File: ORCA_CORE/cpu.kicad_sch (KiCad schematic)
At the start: 0 parts

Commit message: made all sketch for test (cpu board is only for test
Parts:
- added C40, C46, C47: 4.7u, symbol Device:C
- added C44, C48: 1u, symbol Device:C
- added C45: 0.1u, symbol Device:C
- added C49: 1u/50V, symbol Device:C
- added C50: 0.1u25V, symbol Device:C
- added D19: LED_cpu, symbol Device:LED_Filled
- added D20: LED_motor, symbol Device:LED_Filled
- added D22, D25: CUHS20560, symbol Device:D_Schottky
- added D23: LED_usb, symbol Device:D_Filled
- added D24: WS2812B, LED_SMD:LED_WS2812B_PLCC4_5.0x5.0mm_P3.2mm, symbol LED:WS2812B
- added J10: Raspberry_Pi_2_3, Connector_PinSocket_2.54mm:PinSocket_2x20_P2.54mm_Horizontal, symbol Connector:Raspberry_Pi_2_3
- added J11, J12: I2C, symbol Connector_Generic:Conn_01x03
- added J13: 6Vout, symbol Connector_Generic:Conn_01x02
- added J14, J20: 5Vout, symbol Connector_Generic:Conn_01x02
- added J15, J16: Conn_01x05_Pin, symbol Connector:Conn_01x05_Pin
- added P1: USB_C_Plug_USB2.0, symbol Connector:USB_C_Plug_USB2.0
- added Q6, Q7: BSS138, Package_TO_SOT_SMD:SOT-23, symbol Transistor_FET:BSS138
- added R34: 0, symbol Device:R
- added R35, R36, R40: 1k, symbol Device:R
- added R37, R38, R41, R42, R43, R44, R45, R46: 2.2k, symbol Device:R
- added R39: 5.1k, symbol Device:R
- added U13: FT230XS, Package_SO:SSOP-16_3.9x4.9mm_P0.635mm, symbol Interface_USB:FT230XS
- added U14: BNO055, symbol mylib:BNO055
- added U15: NJM78055DL1, symbol mylib:NJM7805SDL1
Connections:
- new net: D22.2 (A), P1.A4 (VBUS), P1.A9 (VBUS), P1.B4 (VBUS), P1.B9 (VBUS), R40.1
- new net: D23.2 (A), R40.2
- new net: P1.A5 (CC), R39.2
- new net: P1.A6 (D+), U13.8 (USBDP)
- new net: P1.A7 (D-), U13.9 (USBDM)
- new net: D20.2 (A), R36.2
- new net: D19.2 (A), R35.2
- new net +3V3_cpu: J10.1 (3V3), J10.17 (3V3), J11.1 (Pin_1), J12.1 (Pin_1), Q6.1 (G), Q7.1 (G), R37.1, R38.1, R41.1, R42.1, R43.1, R44.1, U14.1 (VDD), U14.2 (VDDIO)
- new net +5V_cpu: C40.1, C44.1, C45.1, D22.1 (K), D24.1 (VDD), J10.2 (5V), J10.4 (5V), J14.2 (Pin_2), R35.1, R45.1, R46.1, U13.12 (VCC), U13.3 (VCCIO)
- new net +5V_cpu2servo: C50.1, D25.2 (A), J20.2 (Pin_2), U15.2 (Vout)
- new net +6V_cpu: C46.1, C47.1, C48.1, C49.1, D25.1 (K), J13.2 (Pin_2), R36.1, U15.3 (Vin)
- new net GND: C40.2, C44.2, C45.2, C46.2, C47.2, C48.2, C49.2, C50.2, D19.1 (K), D20.1 (K), D23.1 (K), D24.3 (VSS), J10.14 (GND), J10.20 (GND), J10.25 (GND), J10.30 (GND), J10.34 (GND), J10.39 (GND), J10.6 (GND), J10.9 (GND), J13.1 (Pin_1), J14.1 (Pin_1), J20.1 (Pin_1), P1.A1 (GND), P1.A12 (GND), P1.B1 (GND), P1.B12 (GND), P1.S1 (SHIELD), R34.1, R34.2, R39.1, U13.13 (GND), U13.5 (GND), U14.10 (GND), U14.5 (ADOR), U14.8 (PS0), U14.9 (PS1), U15.1 (GND)
- new net GPIO12: J10.32 (PWM0/GPIO12), J15.1 (Pin_1)
- new net GPIO13: J10.33 (PWM1/GPIO13), J15.2 (Pin_2)
- new net GPIO16: J10.36 (GPIO16), J15.3 (Pin_3)
- new net GPIO17: J10.11 (GPIO17), J15.4 (Pin_4)
- new net GPIO18: J10.12 (GPIO18/PWM0), J15.5 (Pin_5)
- new net GPIO19: J10.35 (GPIO19/MISO1), J16.1 (Pin_1)
- new net GPIO20: J10.38 (GPIO20/MOSI1), J16.2 (Pin_2)
- new net GPIO21: J10.40 (GPIO21/SCLK1), J16.3 (Pin_3)
- new net GPIO26: J10.37 (GPIO26), J16.4 (Pin_4)
- new net GPIO27: J10.13 (GPIO27), J16.5 (Pin_5)
- new net RXD_3V3: J10.10 (GPIO15/RXD), Q7.2 (S), R44.2
- new net RXD_5V: Q7.3 (D), R46.2, U13.4 (RXD)
- new net SCL: J10.5 (SCL/GPIO3), J11.2 (Pin_2), J12.2 (Pin_2), R37.2, R42.2, U14.3 (SCL)
- new net SDA: J10.3 (SDA/GPIO2), J11.3 (Pin_3), J12.3 (Pin_3), R38.2, R41.2, U14.4 (SDA)
- new net TXD_3V3: J10.8 (GPIO14/TXD), Q6.2 (S), R43.2
- new net TXD_5V: Q6.3 (D), R45.2, U13.1 (TXD)
- new net emerg_detector: J10.15 (GPIO22)
- new net emerge_order: J10.16 (GPIO23)
- new net full_color_led: D24.4 (DIN), J10.22 (GPIO25)
- new net power_checker: J10.18 (GPIO24)
- no-connect marks 0 -> 22
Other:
- note added: "DCDC 5V 1.5A"
- note added: "I2C"
- note added: "UART"
- note added: "bno055"
- note added: "full color led"
- note added: "out"
- note added: "power"

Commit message: attach all capacitors
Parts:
- C40, C45, C46, C47, C50: footprint (none) -> Capacitor_SMD:C_0603_1608Metric_Pad1.08x0.95mm_HandSolder
- C44, C48, C49: footprint (none) -> Capacitor_SMD:C_0805_2012Metric_Pad1.18x1.45mm_HandSolder
- D19, D20, D23: footprint (none) -> LED_SMD:LED_0603_1608Metric_Pad1.05x0.95mm_HandSolder
- D22, D25: footprint (none) -> Diode:Diode_US2H
- J15, J16: footprint (none) -> Connector_PinHeader_2.54mm:PinHeader_1x05_P2.54mm_Vertical
- P1: footprint (none) -> Connector_USB:USB_C_Receptacle_HCTL_HC-TYPE-C-16P-01A
- R34, R35, R36, R37, R38, R39, R40, R41, R42, R43, R44, R45, R46: footprint (none) -> Resistor_SMD:R_0603_1608Metric_Pad0.98x0.95mm_HandSolder
- U15: footprint (none) -> Package_TO_SOT_SMD:TO-252-2
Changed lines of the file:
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@@
       (effects (font (size 1.27 1.27)) (justify left))
     )
-    (property "Footprint" "" (at 230.632 31.75 90)
+    (property "Footprint" "Resistor_SMD:R_0603_1608Metric_Pad0.98x0.95mm_HandSolder" (at 230.632 31.75 90)
       (effects (font (size 1.27 1.27)) hide)
     )
@@
       (effects (font (size 1.27 1.27)))
     )
-    (property "Footprint" "" (at 54.61 132.588 90)
+    (property "Footprint" "Resistor_SMD:R_0603_1608Metric_Pad0.98x0.95mm_HandSolder" (at 54.61 132.588 90)
       (effects (font (size 1.27 1.27)) hide)
     )
@@
       (effects (font (size 1.27 1.27)))
     )
-    (property "Footprint" "" (at 30.48 62.992 90)
+    (property "Footprint" "Resistor_SMD:R_0603_1608Metric_Pad0.98x0.95mm_HandSolder" (at 30.48 62.992 90)
       (effects (font (size 1.27 1.27)) hide)
     )
@@
       (effects (font (size 1.27 1.27)) (justify left))
     )
-    (property "Footprint" "" (at 167.3352 140.97 0)
+    (property "Footprint" "Capacitor_SMD:C_0603_1608Metric_Pad1.08x0.95mm_HandSolder" (at 167.3352 140.97 0)
       (effects (font (size 1.27 1.27)) hide)
     )
@@
       (effects (font (size 1.27 1.27)) (justify right))
     )
-    (property "Footprint" "" (at 61.468 156.21 90)
+    (property "Footprint" "Resistor_SMD:R_0603_1608Metric_Pad0.98x0.95mm_HandSolder" (at 61.468 156.21 90)
       (effects (font (size 1.27 1.27)) hide)
     )
@@
       (effects (font (size 1.27 1.27)) (justify left))
     )
-    (property "Footprint" "" (at 107.442 63.5 90)
+    (property "Footprint" "Resistor_SMD:R_0603_1608Metric_Pad0.98x0.95mm_HandSolder" (at 107.442 63.5 90)
       (effects (font (size 1.27 1.27)) hide)
     )
@@
       (effects (font (size 1.27 1.27)))
     )
-    (property "Footprint" "" (at 149.86 123.19 0)
+    (property "Footprint" "Diode:Diode_US2H" (at 149.86 123.19 0)
       (effects (font (size 1.27 1.27)) hide)
     )
@@
       (effects (font (size 1.27 1.27)))
     )
-    (property "Footprint" "" (at 149.86 129.54 0)
+    (property "Footprint" "Package_TO_SOT_SMD:TO-252-2" (at 149.86 129.54 0)
       (effects (font (size 1.27 1.27)) hide)
     )
@@
       (effects (font (size 1.27 1.27)) (justify left))
     )
-    (property "Footprint" "" (at 37.7952 43.18 0)
+    (property "Footprint" "Capacitor_SMD:C_0603_1608Metric_Pad1.08x0.95mm_HandSolder" (at 37.7952 43.18 0)
       (effects (font (size 1.27 1.27)) hide)
     )
@@
       (effects (font (size 1.27 1.27)) (justify left))
     )
-    (property "Footprint" "" (at 121.412 38.1 90)
+    (property "Footprint" "Resistor_SMD:R_0603_1608Metric_Pad0.98x0.95mm_HandSolder" (at 121.412 38.1 90)
       (effects (font (size 1.27 1.27)) hide)
     )
@@
       (effects (font (size 1.27 1.27)) (justify left))
     )
-    (property "Footprint" "" (at 46.6852 43.18 0)
+    (property "Footprint" "Capacitor_SMD:C_0805_2012Metric_Pad1.18x1.45mm_HandSolder" (at 46.6852 43.18 0)
       (effects (font (size 1.27 1.27)) hide)
     )
@@
       (effects (font (size 1.27 1.27)))
     )
-    (property "Footprint" "" (at 58.42 69.088 90)
+    (property "Footprint" "Resistor_SMD:R_0603_1608Metric_Pad0.98x0.95mm_HandSolder" (at 58.42 69.088 90)
       (effects (font (size 1.27 1.27)) hide)
     )
@@
       (effects (font (size 1.27 1.27)))
     )
-    (property "Footprint" "" (at 58.42 56.388 90)
+    (property "Footprint" "Resistor_SMD:R_0603_1608Metric_Pad0.98x0.95mm_HandSolder" (at 58.42 56.388 90)
       (effects (font (size 1.27 1.27)) hide)
     )
@@
       (effects (font (size 1.27 1.27)))
     )
-    (property "Footprint" "" (at 66.04 54.61 0)
+    (property "Footprint" "LED_SMD:LED_0603_1608Metric_Pad1.05x0.95mm_HandSolder" (at 66.04 54.61 0)
       (effects (font (size 1.27 1.27)) hide)
     )
@@
       (effects (font (size 1.27 1.27)))
     )
-    (property "Footprint" "" (at 62.23 130.81 0)
+    (property "Footprint" "LED_SMD:LED_0603_1608Metric_Pad1.05x0.95mm_HandSolder" (at 62.23 130.81 0)
       (effects (font (size 1.27 1.27)) hide)
     )
@@
       (effects (font (size 1.27 1.27)) (justify left))
     )
-    (property "Footprint" "" (at 28.9052 43.18 0)
+    (property "Footprint" "Capacitor_SMD:C_0603_1608Metric_Pad1.08x0.95mm_HandSolder" (at 28.9052 43.18 0)
       (effects (font (size 1.27 1.27)) hide)
     )
@@
       (effects (font (size 1.27 1.27)) (justify left))
     )
-    (property "Footprint" "" (at 37.7952 29.21 0)
+    (property "Footprint" "Capacitor_SMD:C_0805_2012Metric_Pad1.18x1.45mm_HandSolder" (at 37.7952 29.21 0)
       (effects (font (size 1.27 1.27)) hide)
     )
@@
       (effects (font (size 1.27 1.27)))
     )
-    (property "Footprint" "" (at 66.04 67.31 0)
+    (property "Footprint" "LED_SMD:LED_0603_1608Metric_Pad1.05x0.95mm_HandSolder" (at 66.04 67.31 0)
       (effects (font (size 1.27 1.27)) hide)
     )
@@
       (effects (font (size 1.27 1.27)))
     )
-    (property "Footprint" "" (at 242.57 128.27 0)
+    (property "Footprint" "Connector_PinHeader_2.54mm:PinHeader_1x05_P2.54mm_Vertical" (at 242.57 128.27 0)
       (effects (font (size 1.27 1.27)) hide)
     )
@@
       (effects (font (size 1.27 1.27)))
     )
-    (property "Footprint" "" (at 33.02 146.05 0)
+    (property "Footprint" "Connector_USB:USB_C_Receptacle_HCTL_HC-TYPE-C-16P-01A" (at 33.02 146.05 0)
       (effects (font (size 1.27 1.27)) hide)
     )
@@
       (effects (font (size 1.27 1.27)) (justify left))
     )
-    (property "Footprint" "" (at 31.242 90.17 90)
+    (property "Footprint" "Resistor_SMD:R_0603_1608Metric_Pad0.98x0.95mm_HandSolder" (at 31.242 90.17 90)
       (effects (font (size 1.27 1.27)) hide)
     )
@@
       (effects (font (size 1.27 1.27)))
     )
-    (property "Footprint" "" (at 261.62 128.27 0)
+    (property "Footprint" "Connector_PinHeader_2.54mm:PinHeader_1x05_P2.54mm_Vertical" (at 261.62 128.27 0)
       (effects (font (size 1.27 1.27)) hide)
     )
@@
       (effects (font (size 1.27 1.27)) (justify left))
     )
-    (property "Footprint" "" (at 121.412 63.5 90)
+    (property "Footprint" "Resistor_SMD:R_0603_1608Metric_Pad0.98x0.95mm_HandSolder" (at 121.412 63.5 90)
       (effects (font (size 1.27 1.27)) hide)
     )
@@
       (effects (font (size 1.27 1.27)) (justify left))
     )
-    (property "Footprint" "" (at 135.5852 140.97 0)
+    (property "Footprint" "Capacitor_SMD:C_0805_2012Metric_Pad1.18x1.45mm_HandSolder" (at 135.5852 140.97 0)
       (effects (font (size 1.27 1.27)) hide)
     )
@@
       (effects (font (size 1.27 1.27)) (justify left))
     )
-    (property "Footprint" "" (at 46.99 123.19 0)
+    (property "Footprint" "Diode:Diode_US2H" (at 46.99 123.19 0)
       (effects (font (size 1.27 1.27)) hide)
     )
@@
       (effects (font (size 1.27 1.27)) (justify left))
     )
-    (property "Footprint" "" (at 107.442 38.1 90)
+    (property "Footprint" "Resistor_SMD:R_0603_1608Metric_Pad0.98x0.95mm_HandSolder" (at 107.442 38.1 90)
       (effects (font (size 1.27 1.27)) hide)
     )
@@
       (effects (font (size 1.27 1.27)) (justify left))
     )
-    (property "Footprint" "" (at 238.252 31.75 90)
+    (property "Footprint" "Resistor_SMD:R_0603_1608Metric_Pad0.98x0.95mm_HandSolder" (at 238.252 31.75 90)
       (effects (font (size 1.27 1.27)) hide)
     )
@@
       (effects (font (size 1.27 1.27)) (justify left))
     )
-    (property "Footprint" "" (at 40.132 90.17 90)
+    (property "Footprint" "Resistor_SMD:R_0603_1608Metric_Pad0.98x0.95mm_HandSolder" (at 40.132 90.17 90)
       (effects (font (size 1.27 1.27)) hide)
     )
@@
       (effects (font (size 1.27 1.27)) (justify left))
     )
-    (property "Footprint" "" (at 46.6852 29.21 0)
+    (property "Footprint" "Capacitor_SMD:C_0603_1608Metric_Pad1.08x0.95mm_HandSolder" (at 46.6852 29.21 0)
       (effects (font (size 1.27 1.27)) hide)
     )
@@
       (effects (font (size 1.27 1.27)) (justify left))
     )
-    (property "Footprint" "" (at 28.9052 29.21 0)
-      (effects (font (size 1.27 1.27)) hide)
-    )
+    (property "Footprint" "Capacitor_SMD:C_0603_1608Metric_Pad1.08x0.95mm_HandSolder" (at 28.9052 29.21 0)
+      (effects (font (size 1.27 1.27)) hide)
+    )

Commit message: attach all the footprints
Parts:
- R36: footprint Resistor_SMD:R_0603_1608Metric_Pad0.98x0.95mm_HandSolder -> Relay_THT:RH1-U
- U14: footprint (none) -> IMU:BNO055
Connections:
- net +3V3_cpu: no longer U14.2 (VDDIO)
- net GND: now also U14.2 (GND), U14.7 (GND); no longer U14.10 (GND), U14.5 (ADOR), U14.8 (PS0), U14.9 (PS1)
- no-connect marks 22 -> 23
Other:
- moved on the sheet: D22, D23, P1, R39, R40, R41, R42, U13

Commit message: change sketch a little
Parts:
- J11, J12: footprint (none) -> Connector_JST:JST_XH_B3B-XH-A_1x03_P2.50mm_Vertical
- J13, J14, J20: footprint (none) -> Conn:power_pad
- R36: footprint Relay_THT:RH1-U -> Resistor_SMD:R_0603_1608Metric_Pad0.98x0.95mm_HandSolder
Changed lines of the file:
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@@
       (effects (font (size 1.27 1.27)) (justify left))
     )
-    (property "Footprint" "" (at 223.52 129.54 0)
+    (property "Footprint" "Conn:power_pad" (at 223.52 129.54 0)
       (effects (font (size 1.27 1.27)) hide)
     )
@@
       (effects (font (size 1.27 1.27)) (justify left))
     )
-    (property "Footprint" "" (at 223.52 139.7 0)
+    (property "Footprint" "Conn:power_pad" (at 223.52 139.7 0)
       (effects (font (size 1.27 1.27)) hide)
     )
@@
       (effects (font (size 1.27 1.27)))
     )
-    (property "Footprint" "Relay_THT:RH1-U" (at 58.42 69.088 90)
+    (property "Footprint" "Resistor_SMD:R_0603_1608Metric_Pad0.98x0.95mm_HandSolder" (at 58.42 69.088 90)
       (effects (font (size 1.27 1.27)) hide)
     )
@@
       (effects (font (size 1.27 1.27)) (justify right))
     )
-    (property "Footprint" "" (at 64.77 86.36 0)
+    (property "Footprint" "Connector_JST:JST_XH_B3B-XH-A_1x03_P2.50mm_Vertical" (at 64.77 86.36 0)
       (effects (font (size 1.27 1.27)) hide)
     )
@@
       (effects (font (size 1.27 1.27)) (justify left))
     )
-    (property "Footprint" "" (at 223.52 119.38 0)
+    (property "Footprint" "Conn:power_pad" (at 223.52 119.38 0)
       (effects (font (size 1.27 1.27)) hide)
     )
@@
       (effects (font (size 1.27 1.27)) (justify right))
     )
-    (property "Footprint" "" (at 73.66 86.36 0)
-      (effects (font (size 1.27 1.27)) hide)
-    )
+    (property "Footprint" "Connector_JST:JST_XH_B3B-XH-A_1x03_P2.50mm_Vertical" (at 73.66 86.36 0)
+      (effects (font (size 1.27 1.27)) hide)
+    )

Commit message: plate power
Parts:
- added H10, H11, H12: Hole_cup, MountingHole:MountingHole_3.2mm_M3, symbol Mechanical:MountingHole
- added H9: Hole_cpu, MountingHole:MountingHole_3.2mm_M3, symbol Mechanical:MountingHole

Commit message: plate power and usp
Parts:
- added Q8: BSS138, Package_TO_SOT_SMD:SOT-23, symbol Transistor_FET:BSS138
- added R6: 2.2k, Resistor_SMD:R_0603_1608Metric_Pad0.98x0.95mm_HandSolder, symbol Device:R
- P1: footprint Connector_USB:USB_C_Receptacle_HCTL_HC-TYPE-C-16P-01A -> Connector_USB:USB_C_Receptacle_HCTL_HC-TYPE-C-16P-01A_withmodel
- R34: value 0 -> 2.2k
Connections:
- net +3V3_cpu: now also Q8.1 (G), R6.1
- net +5V_cpu: now also R34.1
- net GND: no longer C40.2, C44.2, C45.2, D19.1 (K), D23.1 (K), D24.3 (VSS), J10.14 (GND), J10.20 (GND), J10.25 (GND), J10.30 (GND), J10.34 (GND), J10.39 (GND), J10.6 (GND), J10.9 (GND), J14.1 (Pin_1), P1.A1 (GND), P1.A12 (GND), P1.B1 (GND), P1.B12 (GND), P1.S1 (SHIELD), R34.1, R34.2, R39.1, U13.13 (GND), U13.5 (GND), U14.2 (GND), U14.7 (GND)
- net full_color_led renamed full_color_led_3V3
- net full_color_led_3V3: now also Q8.2 (S), R6.2; no longer D24.4 (DIN)
- new net GND1: C40.2, C44.2, C45.2, D19.1 (K), D23.1 (K), D24.3 (VSS), J10.14 (GND), J10.20 (GND), J10.25 (GND), J10.30 (GND), J10.34 (GND), J10.39 (GND), J10.6 (GND), J10.9 (GND), J14.1 (Pin_1), P1.A1 (GND), P1.A12 (GND), P1.B1 (GND), P1.B12 (GND), P1.S1 (SHIELD), R39.1, U13.13 (GND), U13.5 (GND), U14.2 (GND), U14.7 (GND)
- new net full_color_led_5V: D24.4 (DIN), Q8.3 (D), R34.2
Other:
- moved on the sheet: D24

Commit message: plate all parts
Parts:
- removed H11, H12: Hole_cup, MountingHole:MountingHole_3.2mm_M3, symbol Mechanical:MountingHole
- removed J14: 5Vout, Conn:power_pad, symbol Connector_Generic:Conn_01x02
- added R47, R48, R49: 2.2k, Resistor_SMD:R_0603_1608Metric_Pad0.98x0.95mm_HandSolder, symbol Device:R
- J10: footprint Connector_PinSocket_2.54mm:PinSocket_2x20_P2.54mm_Horizontal -> cpu:raspberrypi_Zero_W_Vertical
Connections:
- net GND1: now also R47.2, R48.2, R49.2
- net SCL: now also R41.2, U14.4 (SCL); no longer R42.2, U14.3 (SDA)
- net SDA: now also R42.2, U14.3 (SDA); no longer R41.2, U14.4 (SCL)
- net emerg_detector: now also R49.1
- net emerge_order: now also R48.1
- net power_checker: now also R47.1
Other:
- moved on the sheet: J20, Q6, Q7, R43, R44, R45, R46

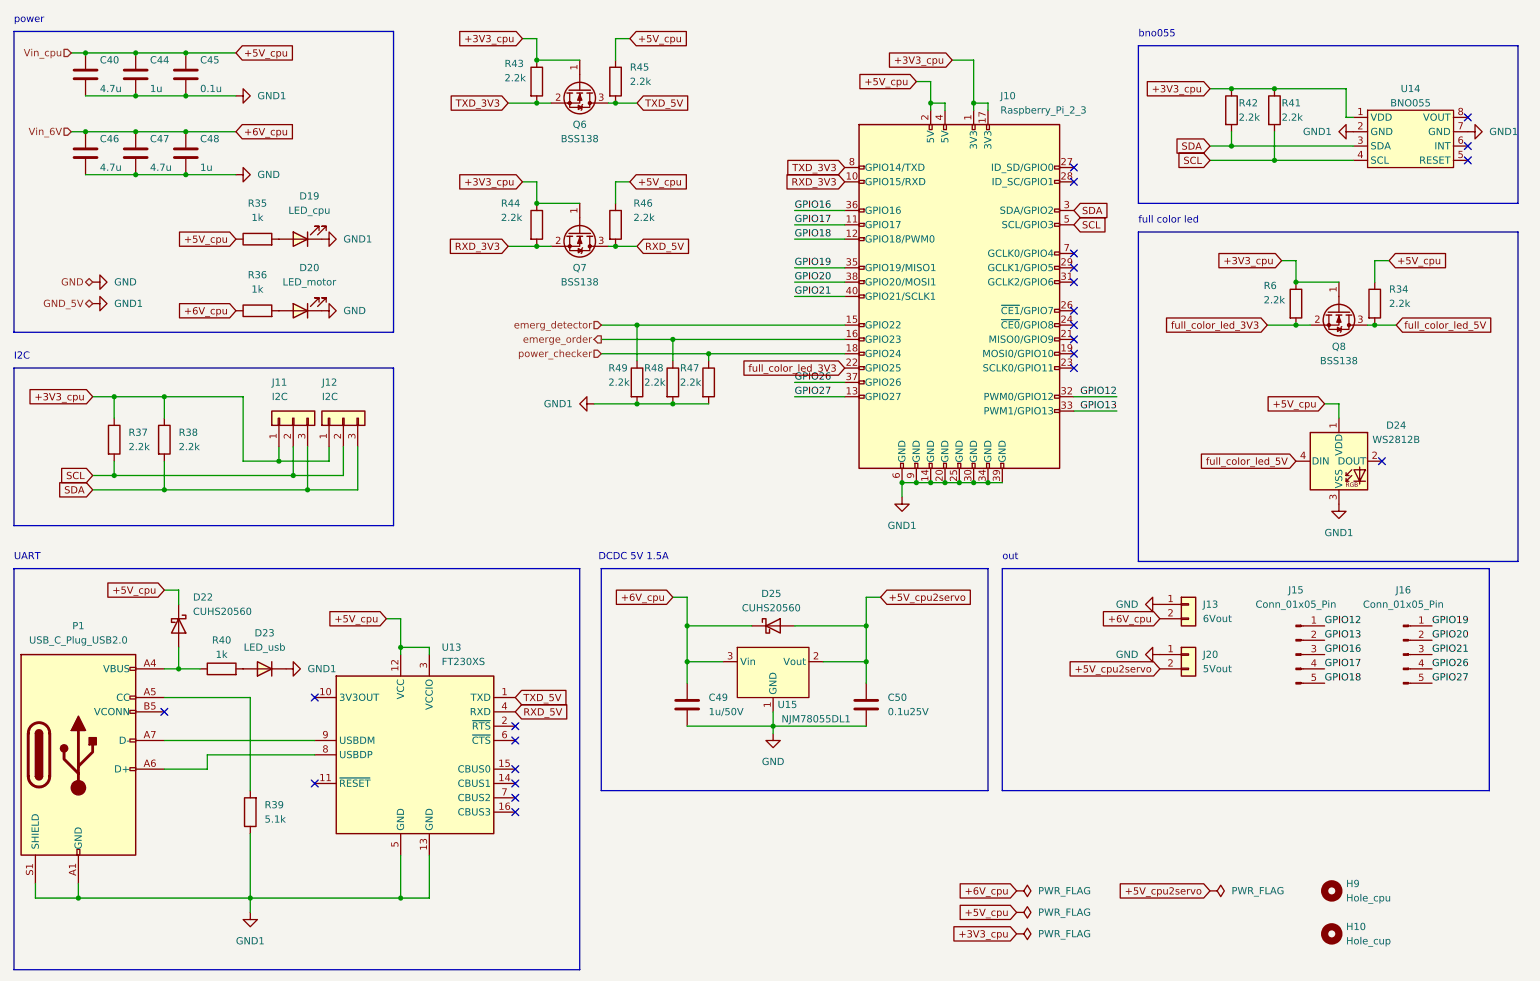
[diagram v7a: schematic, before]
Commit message: complete wireing and filling usp
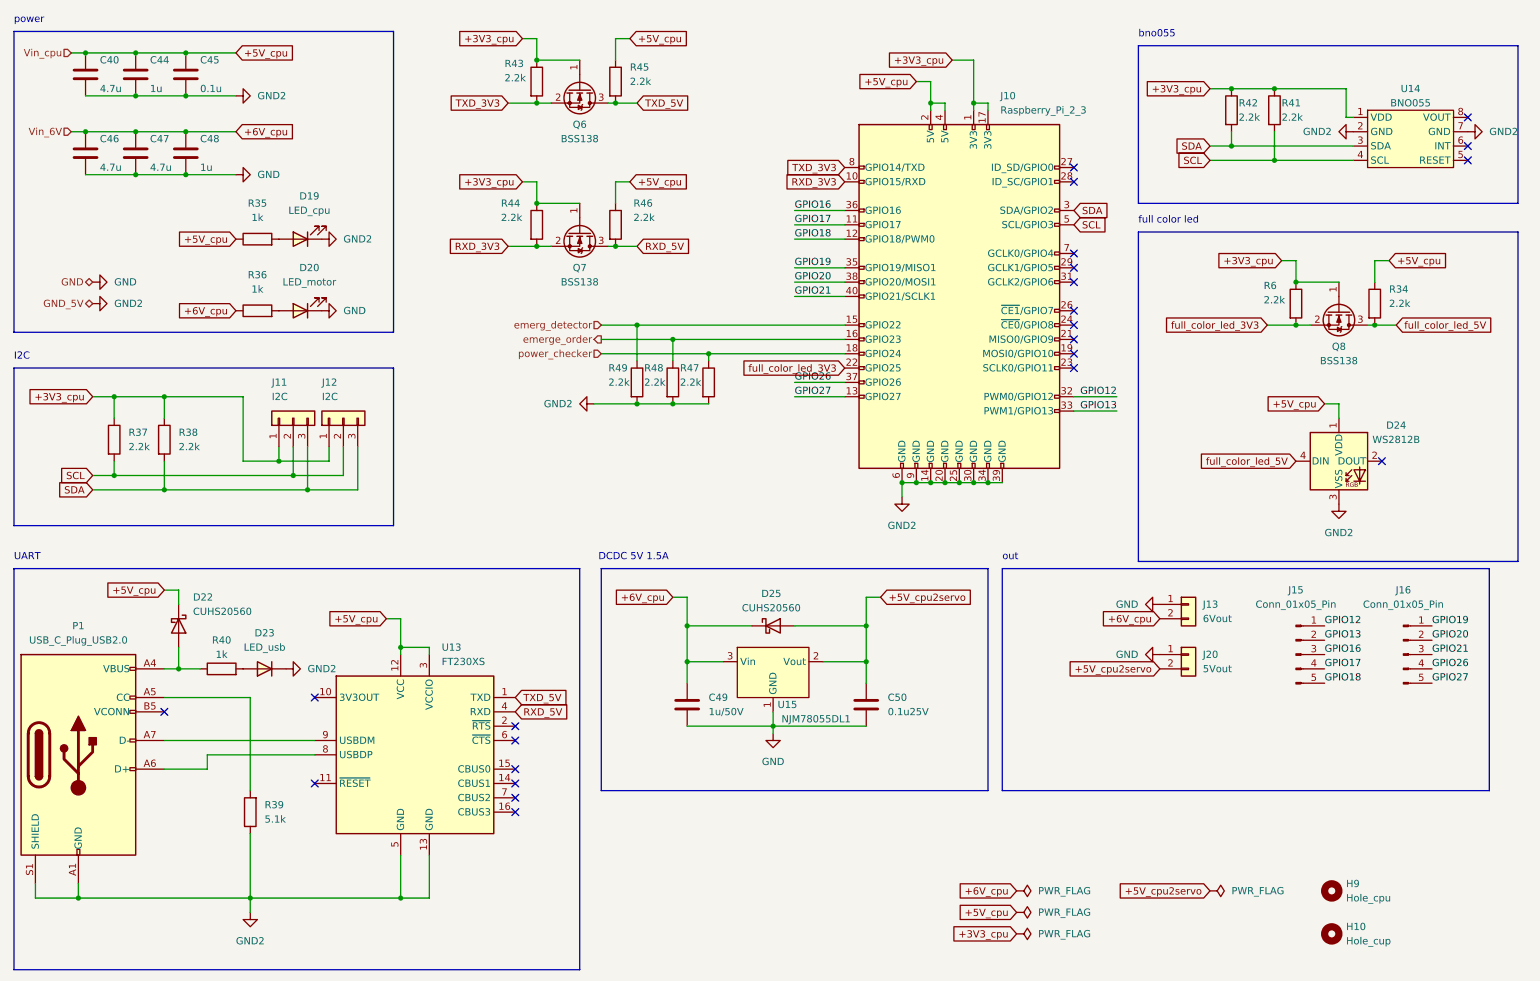
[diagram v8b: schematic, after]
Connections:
- net GND1 renamed GND2
